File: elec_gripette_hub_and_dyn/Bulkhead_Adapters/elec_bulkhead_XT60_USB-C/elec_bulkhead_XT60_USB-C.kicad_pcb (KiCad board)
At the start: 2 copper layers, 14 x 14 mm, 9 parts, among them J1 JST EH 2, J2 USB-C Rec. Vert.

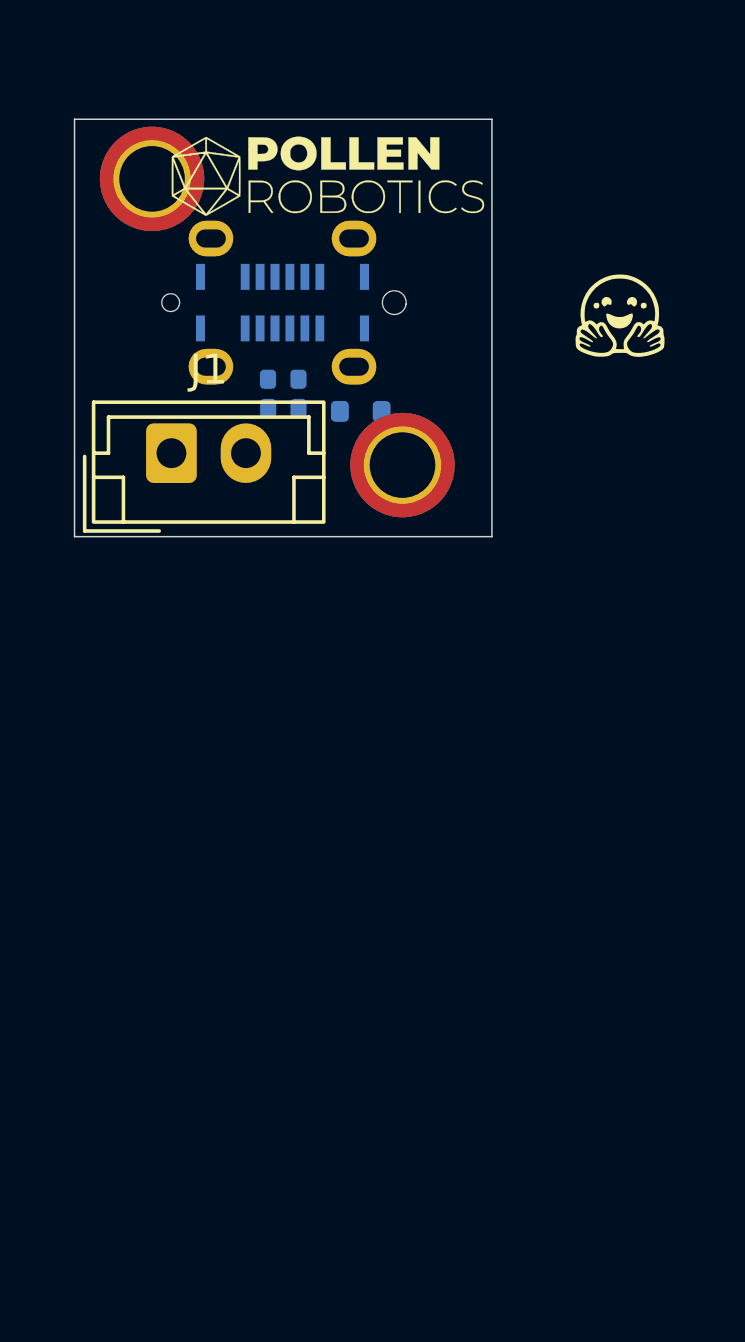
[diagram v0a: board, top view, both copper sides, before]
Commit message: [added] XT60-USB-C Bulkhead for Gripette, JLC ready.
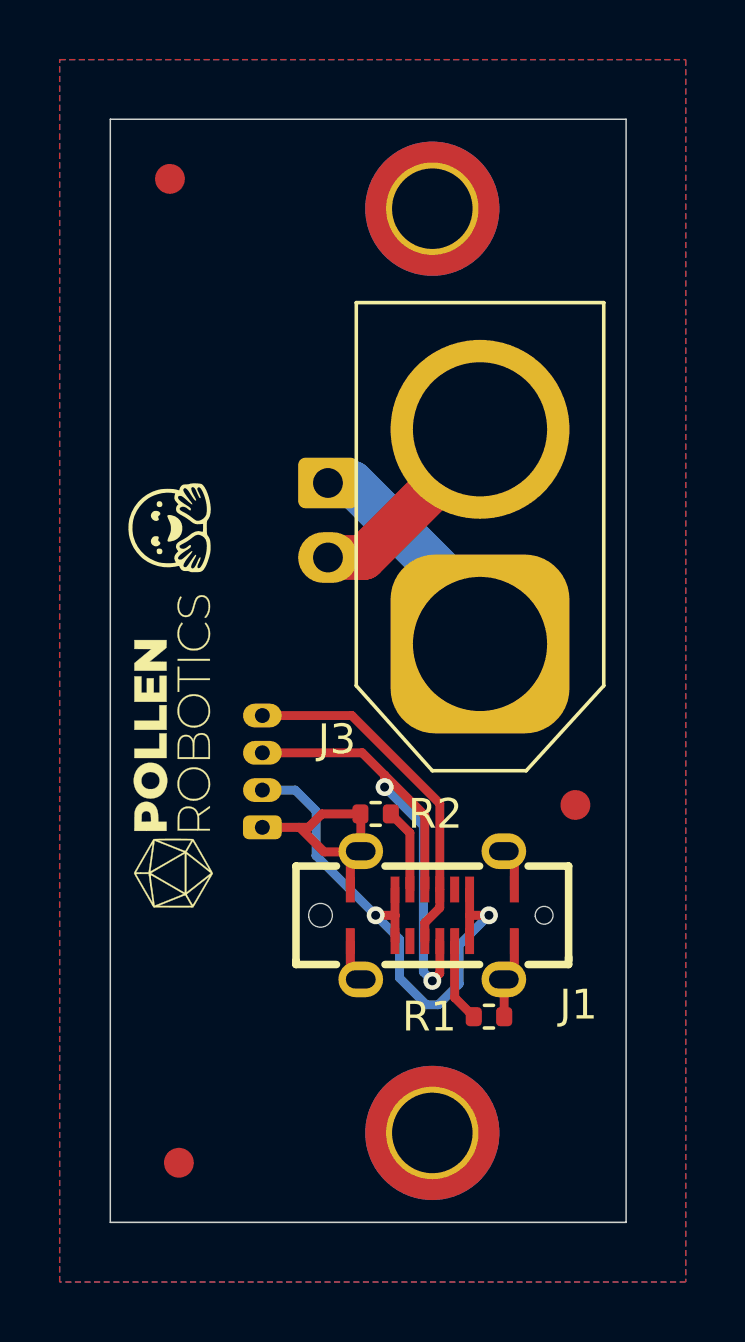
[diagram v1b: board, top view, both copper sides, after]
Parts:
- removed D3: ESD5Z6.0, Diode_SMD:D_SOD-523
- added FID1: DNP Fiducial, Fiducial:Fiducial_1mm_Mask2mm, F.Cu at (82.1, 46.6)
- added FID2: DNP Fiducial, Fiducial:Fiducial_1mm_Mask2mm, F.Cu at (95.7, 67.6)
- added FID3: DNP Fiducial, Fiducial:Fiducial_1mm_Mask2mm, F.Cu at (82.4, 79.6)
- added J3: XT60, Connector_AMASS:AMASS_XT60-M_1x02_P7.20mm_Vertical, F.Cu at (92.5, 62.2)
- added J4: pico4, Connector_Molex:Molex_PicoBlade_53048-0410_1x04_P1.25mm_Horizontal, B.Cu at (85.2, 68.4)
- H4, H5: value Mounting Holes M2 -> Mounting Hole M2,5; footprint MountingHole:MountingHole_2.2mm_M2_ISO7380_Pad_TopBottom -> MountingHole:MountingHole_2.7mm_M2.5_ISO14580_Pad_TopBottom
- J1: value JST EH 2 -> USB-C Rec. Vert.; footprint Connector_JST:JST_EH_B2B-EH-A_1x02_P2.50mm_Vertical -> Library_Pollen:USB-C_16p_vert_Shou-Han_TYPE-C 16P LTH6.8 - C5187468
- J2: value USB-C Rec. Vert. -> JST EH 2; footprint Library_Pollen:USB-C_16p_vert_Shou-Han_TYPE-C 16P LTH6.8 - C5187468 -> Connector_JST:JST_EH_S2B-EH_1x02_P2.50mm_Horizontal
- R1, R2: moved to F.Cu
- moved R1 22.5 mm to (92.8, 74.7), turned to 0 degrees
- moved H5 22.4 mm to (90.9, 78.6)
- moved H3 22.2 mm to (80.5, 65.9), turned to 90 degrees
- moved J1 17.8 mm to (90.9, 71.3), turned to 180 degrees
- moved H2 16.7 mm to (82.1, 58.3), turned to 90 degrees
- moved R2 13.9 mm to (89.0, 67.9)
- moved H4 9.45 mm to (90.9, 47.6)
- moved J2 6.24 mm to (87.4, 56.8), turned to -90 degrees
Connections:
- R1 pad 1: Net-(J2-CC1) -> Net-(J1-CC1)
- R2 pad 1: Net-(J2-CC2) -> Net-(J1-CC2)
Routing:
- net GND: track 0.00 -> 22.1 mm
- net VBUS: track 0.00 -> 19.0 mm, vias 0 -> 2
- net /DM+: track 0.00 -> 17.8 mm, vias 0 -> 2
- net /DM-: track 0.00 -> 12.0 mm
- net +BATT: track 0.00 -> 7.12 mm
- net Net-(J1-CC2): track 0.00 -> 2.80 mm
- net Net-(J1-CC1): track 0.00 -> 2.80 mm
- added copper zone on B.Cu, net GND
- added copper zone on F.Cu, net GND
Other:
- board size 14 x 14 mm -> 17.3 x 37 mm

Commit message: [update] Gripette bulkhead ready for production.
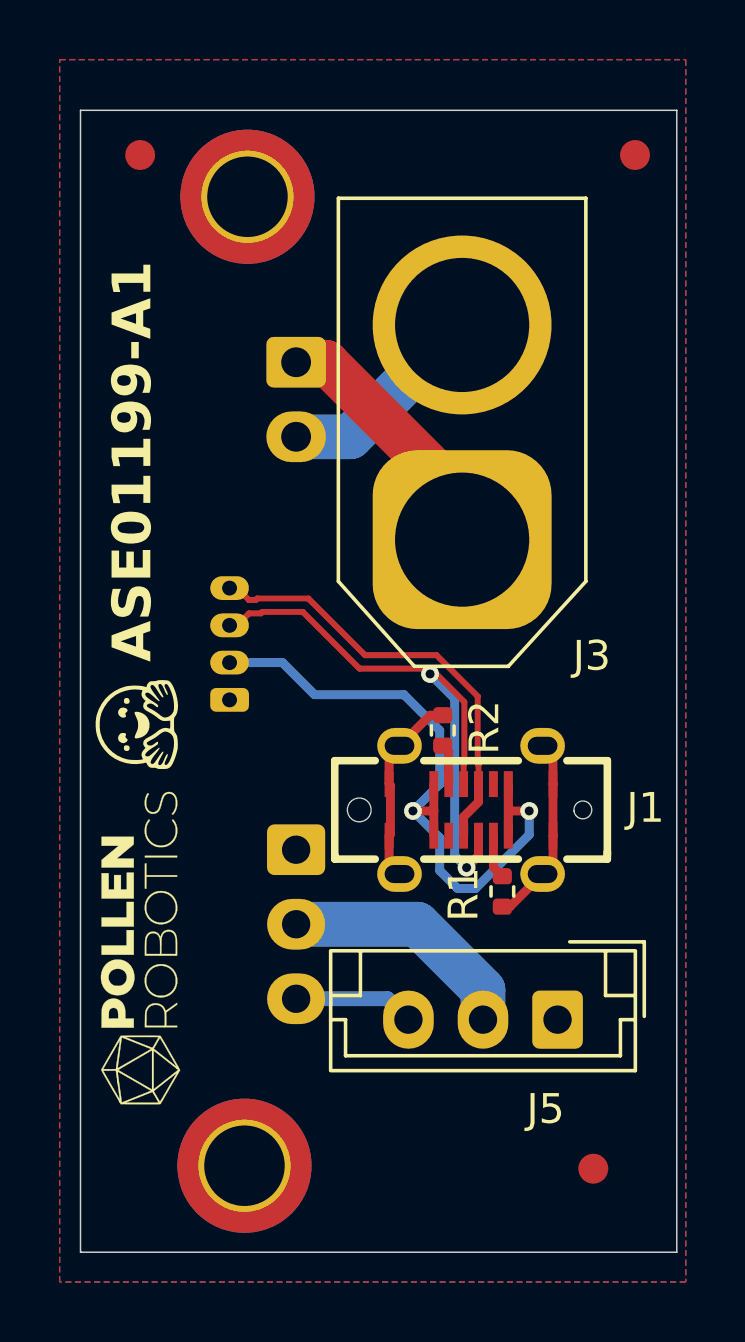
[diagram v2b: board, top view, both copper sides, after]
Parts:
- added J5: Dynamixel-3, Connector_JST:JST_EH_B3B-EH-A_1x03_P2.50mm_Vertical, F.Cu at (95.1, 74.8)
- added J9: Dynamixel-3, Connector_JST:JST_EH_S3B-EH_1x03_P2.50mm_Horizontal, B.Cu at (86.3, 69.1)
- moved FID2 21.9 mm to (97.7, 45.8)
- moved FID3 13.9 mm to (96.3, 79.8)
- moved H2 6.69 mm to (81.0, 64.9)
- moved H3 6.69 mm to (79.4, 72.5)
- moved H5 6.40 mm to (84.6, 79.7)
- moved H4 6.21 mm to (84.7, 47.2)
- moved J4 4.41 mm to (84.1, 64.1)
- moved R1 4.22 mm to (93.2, 70.5), turned to -90 degrees
- moved J2 4.19 mm to (86.3, 52.8)
- moved J1 3.77 mm to (92.2, 67.8)
- moved R2 3.59 mm to (91.2, 65.1), turned to 90 degrees
- moved J3 3.55 mm to (91.9, 58.7)
- moved FID1 1.28 mm to (81.1, 45.8)
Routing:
- net Net-(J5-Pin_2): track 0.00 -> 8.18 mm
- net VBUS: track 19.0 -> 23.1 mm
- net Net-(J5-Pin_3): track 0.00 -> 4.06 mm
- net /DM-: track 12.0 -> 14.8 mm
- net /DM+: track 17.8 -> 20.3 mm
- net Net-(J1-CC2): track 2.80 -> 1.37 mm
- net Net-(J1-CC1): track 2.80 -> 1.48 mm
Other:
- board size 17.3 x 37 mm -> 20 x 38.3 mm
- board text added: "ASE01199-A1"
